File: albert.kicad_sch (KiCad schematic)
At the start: 10 parts, among them J1 Conn_02x10_Odd_Even, J2 USB_C_Receptacle_USB2.0_14P, U2 W25Q32JVSS, U3 USBLC6-2P6

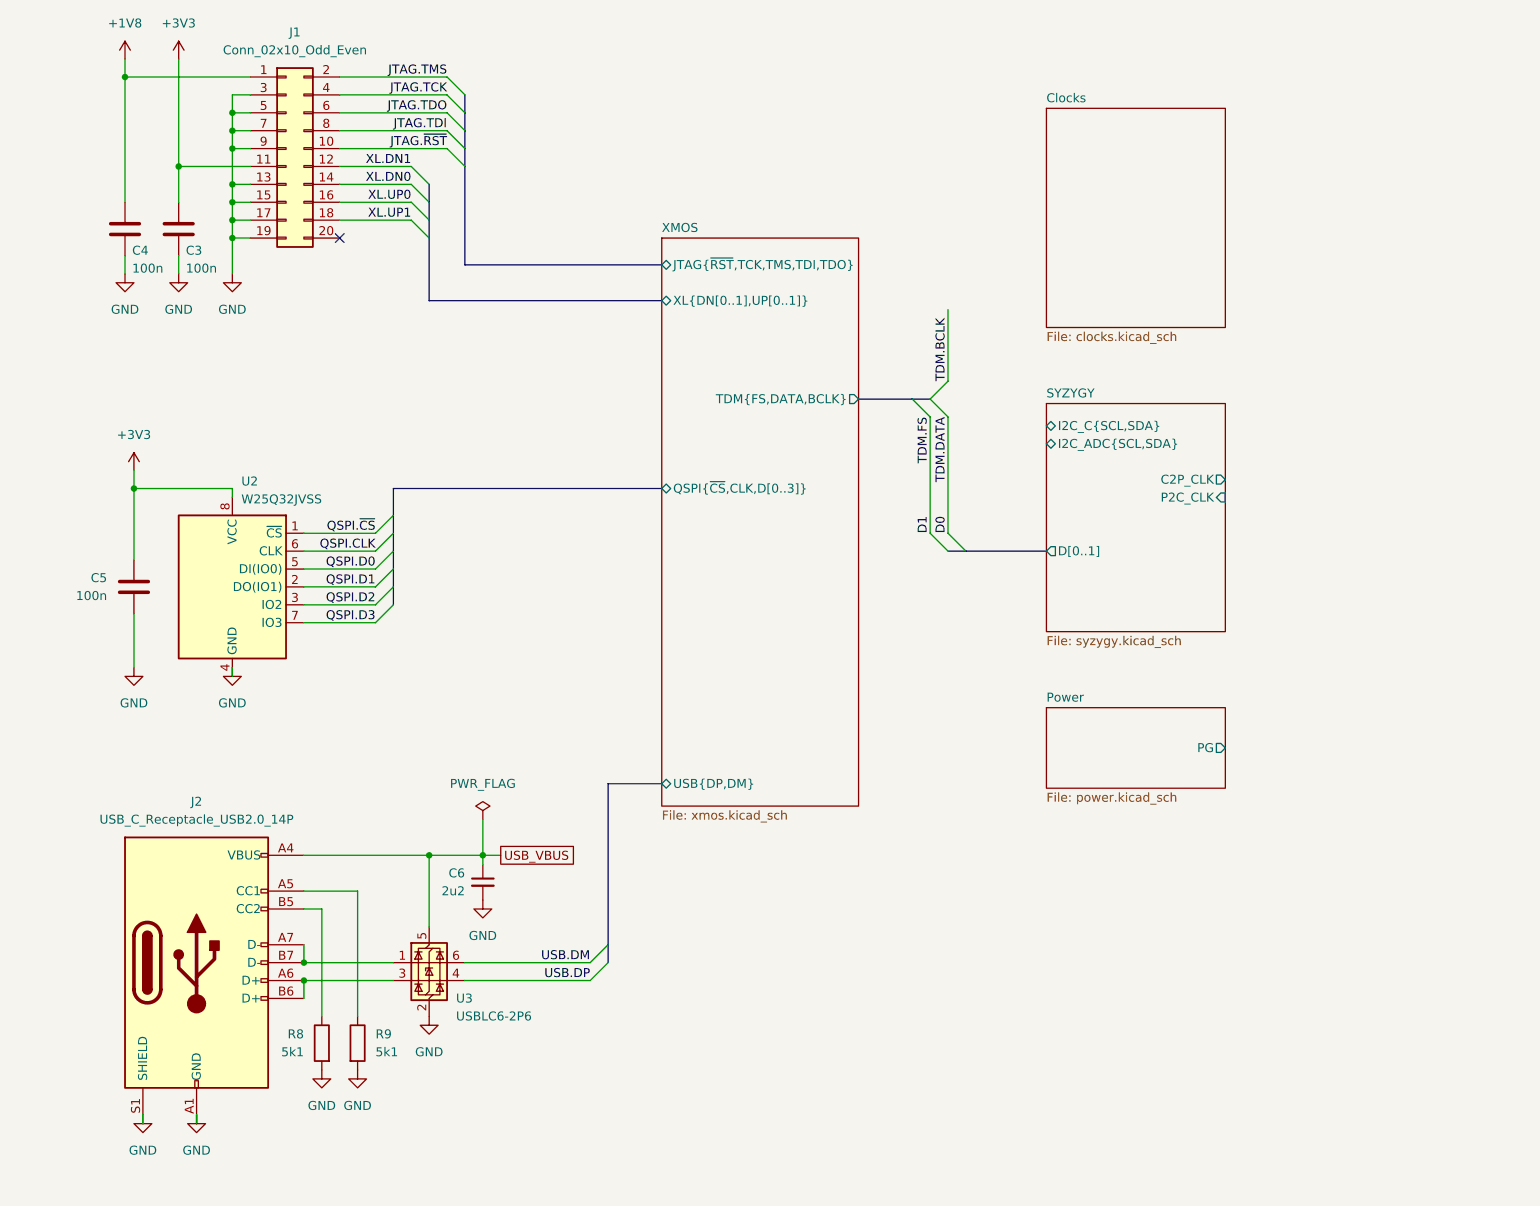
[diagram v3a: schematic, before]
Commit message: Added pMCU
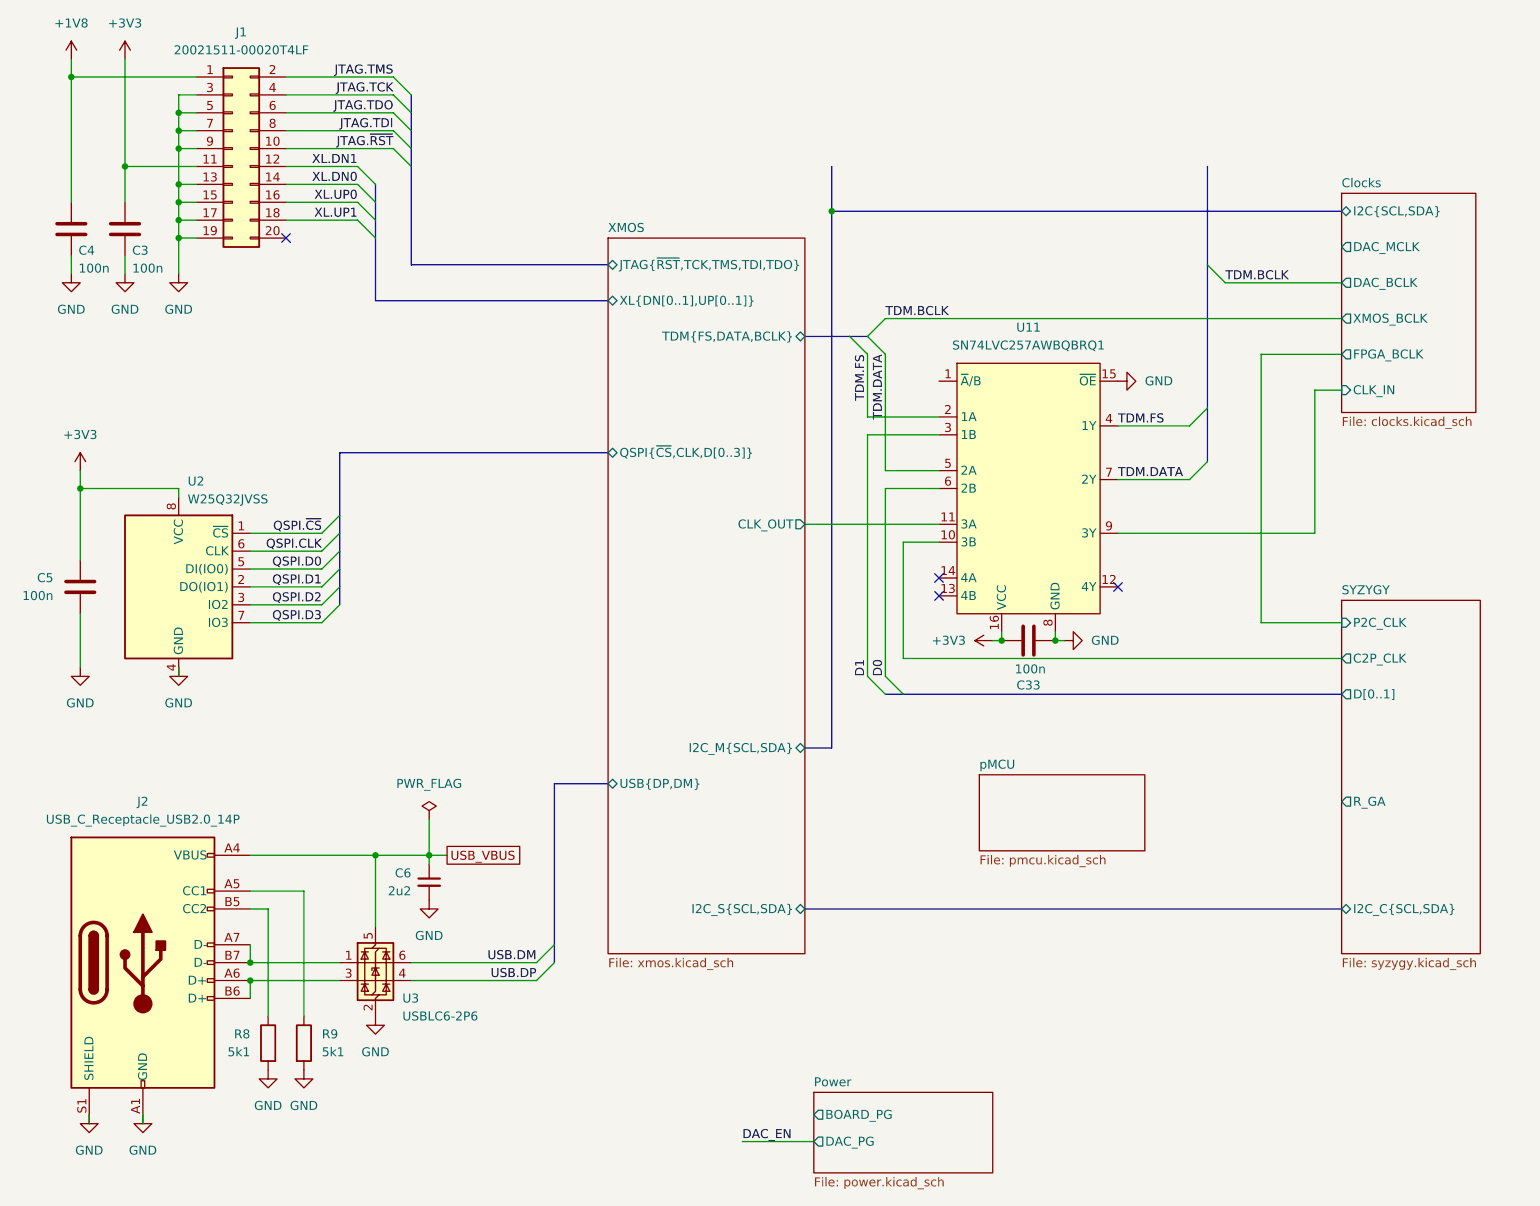
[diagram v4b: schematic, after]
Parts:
- added C33: 100n, symbol Device:C
- added U11: SN74LVC257AWBQBRQ1, Package_DFN_QFN:DHVQFN-16-1EP_2.5x3.5mm_P0.5mm_EP1x2mm, symbol albert-custom:SN74LVC257A
- J1: value Conn_02x10_Odd_Even -> 20021511-00020T4LF
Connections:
- net +3V3: now also C33.1, U11.16 (VCC)
- net D0: now also U11.6 (2B)
- net D1: now also U11.3 (1B)
- net GND: now also C33.2, U11.15 (~{OE}), U11.8 (GND)
- net SYZYGY/C2P_CLK: now also U11.10 (3B)
- new net Clocks/CLK_IN: U11.9 (3Y)
- new net TDM.DATA: U11.5 (2A), U11.7 (2Y)
- new net TDM.FS: U11.2 (1A), U11.4 (1Y)
- new net XMOS/CLK_OUT: U11.11 (3A)
- no-connect marks 1 -> 4
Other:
- added sheet pMCU (pmcu.kicad_sch)
- sheet Clocks ports: added CLK_IN, DAC_BCLK, DAC_MCLK, FPGA_BCLK, I2C{SCL,SDA}, XMOS_BCLK; removed none
- sheet Power ports: added BOARD_PG, DAC_PG; removed PG
- sheet SYZYGY ports: added R_GA; removed I2C_ADC{SCL,SDA}
- sheet XMOS ports: added CLK_OUT, I2C_M{SCL,SDA}, I2C_S{SCL,SDA}; removed none
- moved on the sheet: C3, C4, C5, C6, J1, J2, R8, R9, U2, U3
